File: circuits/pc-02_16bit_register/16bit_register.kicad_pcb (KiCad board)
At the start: 2 copper layers, 99.1 x 99.1 mm, 26 parts, among them U1 74HC273, U2 74HC273, U3 74HC244, U4 74HC244, U5 74HC244, U6 74HC244

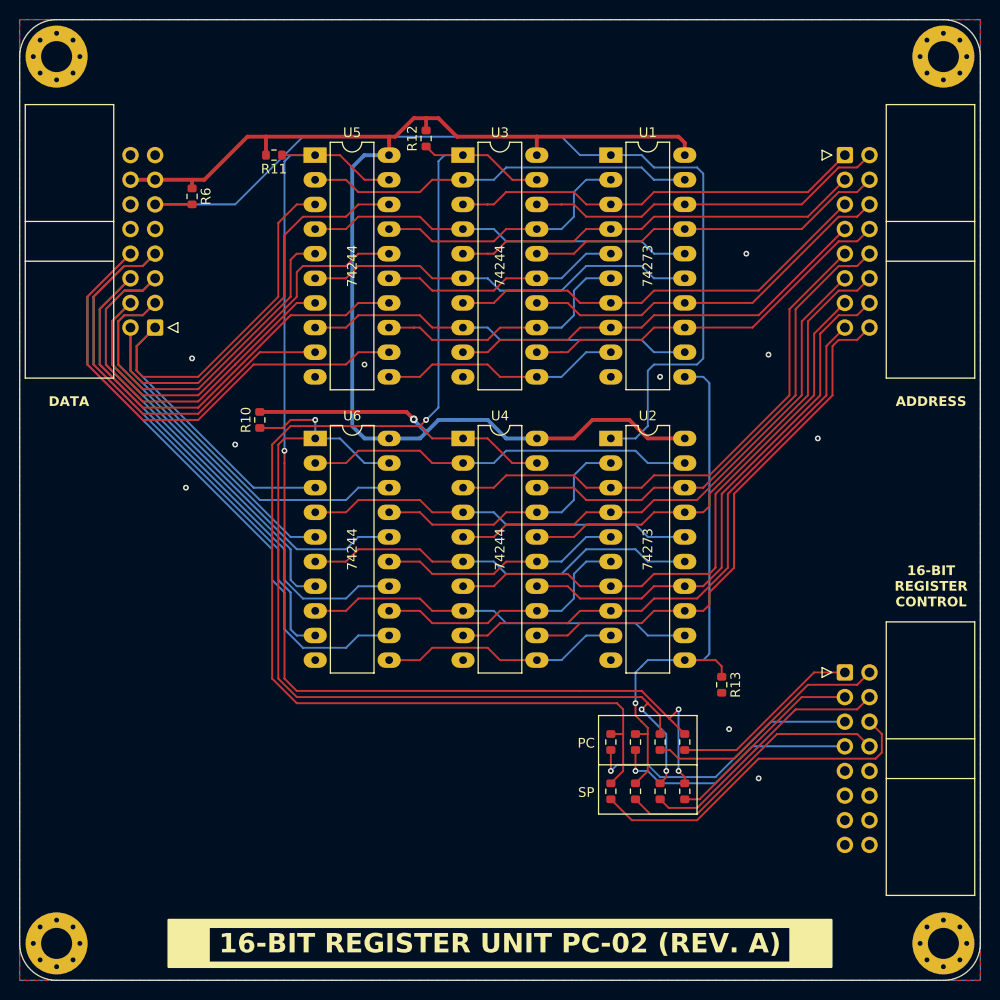
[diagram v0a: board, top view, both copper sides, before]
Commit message: add filter and decoupling capacitors to all boards
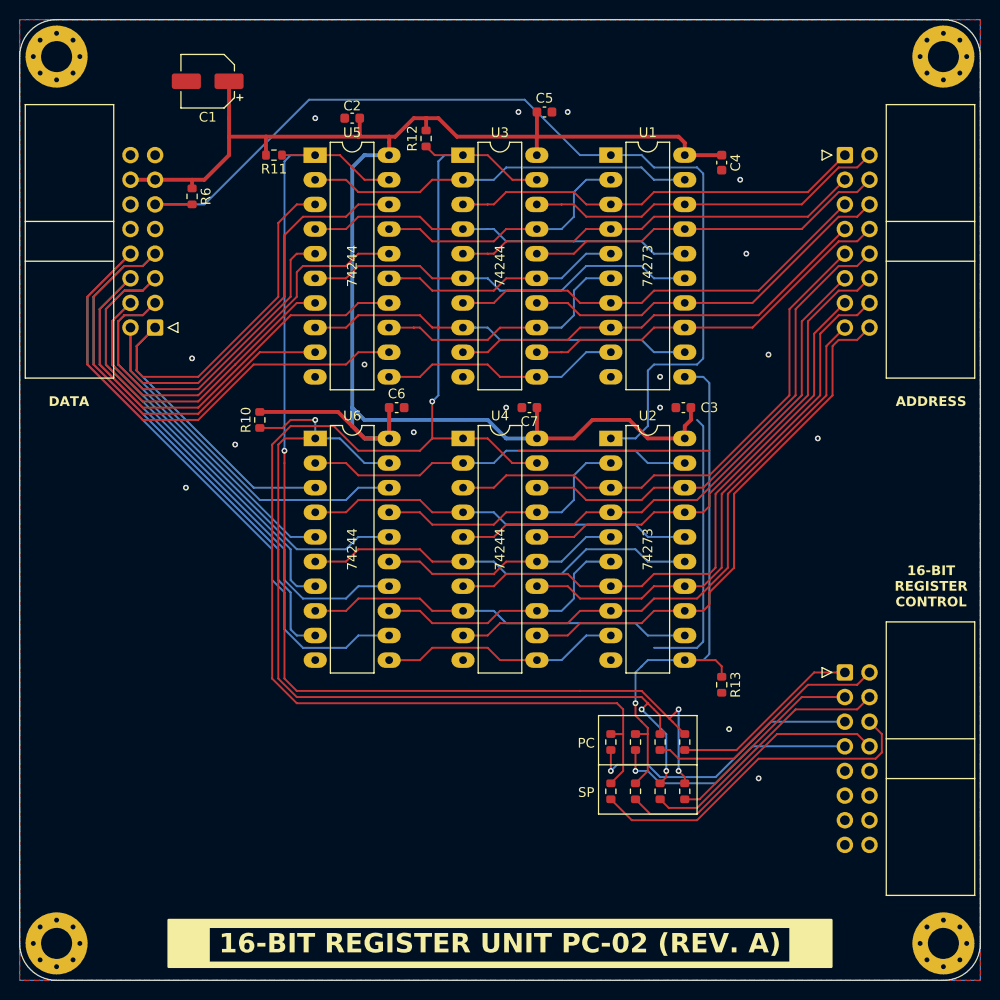
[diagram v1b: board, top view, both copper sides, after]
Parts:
- added C1: C_Polarized, Capacitor_SMD:CP_Elec_5x5.3, F.Cu at (60.0, 29.2)
- added C2: C, Capacitor_SMD:C_0603_1608Metric, F.Cu at (74.9, 33.0)
- added C3: C, Capacitor_SMD:C_0603_1608Metric, F.Cu at (109.1, 62.9)
- added C4: C, Capacitor_SMD:C_0603_1608Metric, F.Cu at (113.0, 37.6)
- added C5: C, Capacitor_SMD:C_0603_1608Metric, F.Cu at (94.8, 32.4)
- added C6: C, Capacitor_SMD:C_0603_1608Metric, F.Cu at (79.5, 62.9)
- added C7: C, Capacitor_SMD:C_0603_1608Metric, F.Cu at (93.2, 62.9)
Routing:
- net GND: track 0.00 -> 28.5 mm, vias 10 -> 17
- net VCC: track 157.0 -> 183.8 mm, vias 1 -> 0
- net /~{reset}: track 100.1 -> 103.3 mm
- net /read16: track 144.4 -> 146.2 mm

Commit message: final touches, pcb ordering
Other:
- board text added: "74244 (DRIVER)"
- board text added: "74273 (REGISTER)"
- board text removed: "74244"
- board text removed: "74273"
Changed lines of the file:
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@@
 		(tenting front back)
 		(pcbplotparams
-			(layerselection 0x00000000_00000000_55555555_575555ff)
+			(layerselection 0x00000000_00000000_55555555_5755f5ff)
 			(plot_on_all_layers_selection 0x00000000_00000000_00000000_00000000)
 			(disableapertmacros no)
-			(usegerberextensions yes)
+			(usegerberextensions no)
 			(usegerberattributes no)
-			(usegerberadvancedattributes yes)
+			(usegerberadvancedattributes no)
 			(creategerberjobfile no)
 			(dashed_line_dash_ratio 12.000000)
@@
 			(sketchdnponfab yes)
 			(crossoutdnponfab yes)
-			(subtractmaskfromsilk no)
+			(subtractmaskfromsilk yes)
 			(outputformat 1)
 			(mirror no)
 			(drillshape 0)
 			(scaleselection 1)
-			(outputdirectory "")
+			(outputdirectory "./CAM")
 		)
 	)
@@
 		(tags "capacitor")
 		(property "Reference" "C6"
-			(at 0 -1.43 0)
+			(at -2.68 0 0)
 			(layer "F.SilkS")
 			(effects
@@
 		(tags "capacitor")
 		(property "Reference" "C7"
-			(at 0 -1.43 0)
+			(at -2.68 0 0)
 			(layer "F.SilkS")
 			(effects
@@
 		)
 	)
-	(gr_text "74244"
+	(gr_text "74244 (DRIVER)"
 		(at 90.17 77.47 90)
 		(layer "F.SilkS")
@@
 		)
 	)
-	(gr_text "74244"
+	(gr_text "74244 (DRIVER)"
 		(at 90.17 48.26 90)
 		(layer "F.SilkS")
@@
 		)
 	)
-	(gr_text "74273"
+	(gr_text "74273 (REGISTER)"
 		(at 105.41 77.47 90)
 		(layer "F.SilkS")
@@
 		)
 	)
-	(gr_text "74273"
+	(gr_text "74273 (REGISTER)"
 		(at 105.41 48.26 90)
 		(layer "F.SilkS")
@@
 		)
 	)
-	(gr_text "74244"
+	(gr_text "74244 (DRIVER)"
 		(at 74.93 48.26 90)
 		(layer "F.SilkS")
@@
 		)
 	)
-	(gr_text "74244"
+	(gr_text "74244 (DRIVER)"
 		(at 74.93 77.47 90)
 		(layer "F.SilkS")

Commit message: pcb design
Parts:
- added R14: 0R, Resistor_SMD:R_0603_1608Metric, F.Cu at (104.1, 107.5)
- added R15: 0R, Resistor_SMD:R_0603_1608Metric, F.Cu at (109.2, 107.5)
- added R16: 0R, Resistor_SMD:R_0603_1608Metric, F.Cu at (106.7, 107.5)
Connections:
- CTRL_BUS1 pad 12: unconnected-(CTRL_BUS1-Pin_12-Pad12) -> /writeIPC
- CTRL_BUS1 pad 13: unconnected-(CTRL_BUS1-Pin_13-Pad13) -> /~{readIPC_low}
- CTRL_BUS1 pad 14: unconnected-(CTRL_BUS1-Pin_14-Pad14) -> /~{readIPC_high}
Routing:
- net /writeIPC: track 0.00 -> 37.7 mm
- net /~{readIPC_high}: track 0.00 -> 30.8 mm
- net /~{read8low}: track 121.7 -> 146.5 mm, vias 3 -> 5
- net /~{readIPC_low}: track 0.00 -> 19.5 mm
- net /write16: track 58.1 -> 77.5 mm, vias 1 -> 2
- net /~{read8high}: track 97.5 -> 114.0 mm, vias 3 -> 4
- net GND: vias 17 -> 16
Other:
- board text added: "*74244 (DRIVER)"
- board text added: "*U3/U4 not required for IPC config"
- board text added: "16-BIT REGISTER UNIT PC-02 (REV. B)"
- board text added: "IPC"
- board text removed: "16-BIT REGISTER UNIT PC-02 (REV. A)"
